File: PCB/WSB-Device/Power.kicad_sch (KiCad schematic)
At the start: 38 parts, among them J3 USB_C_Receptacle_USB2.0_14P, J4 Conn_01x02, SW2 SW_SPST_4_PIN, U2 XC6194A303ER-G, U3 USBLC6-2P6, U4 MCP73830, U6 NCP187

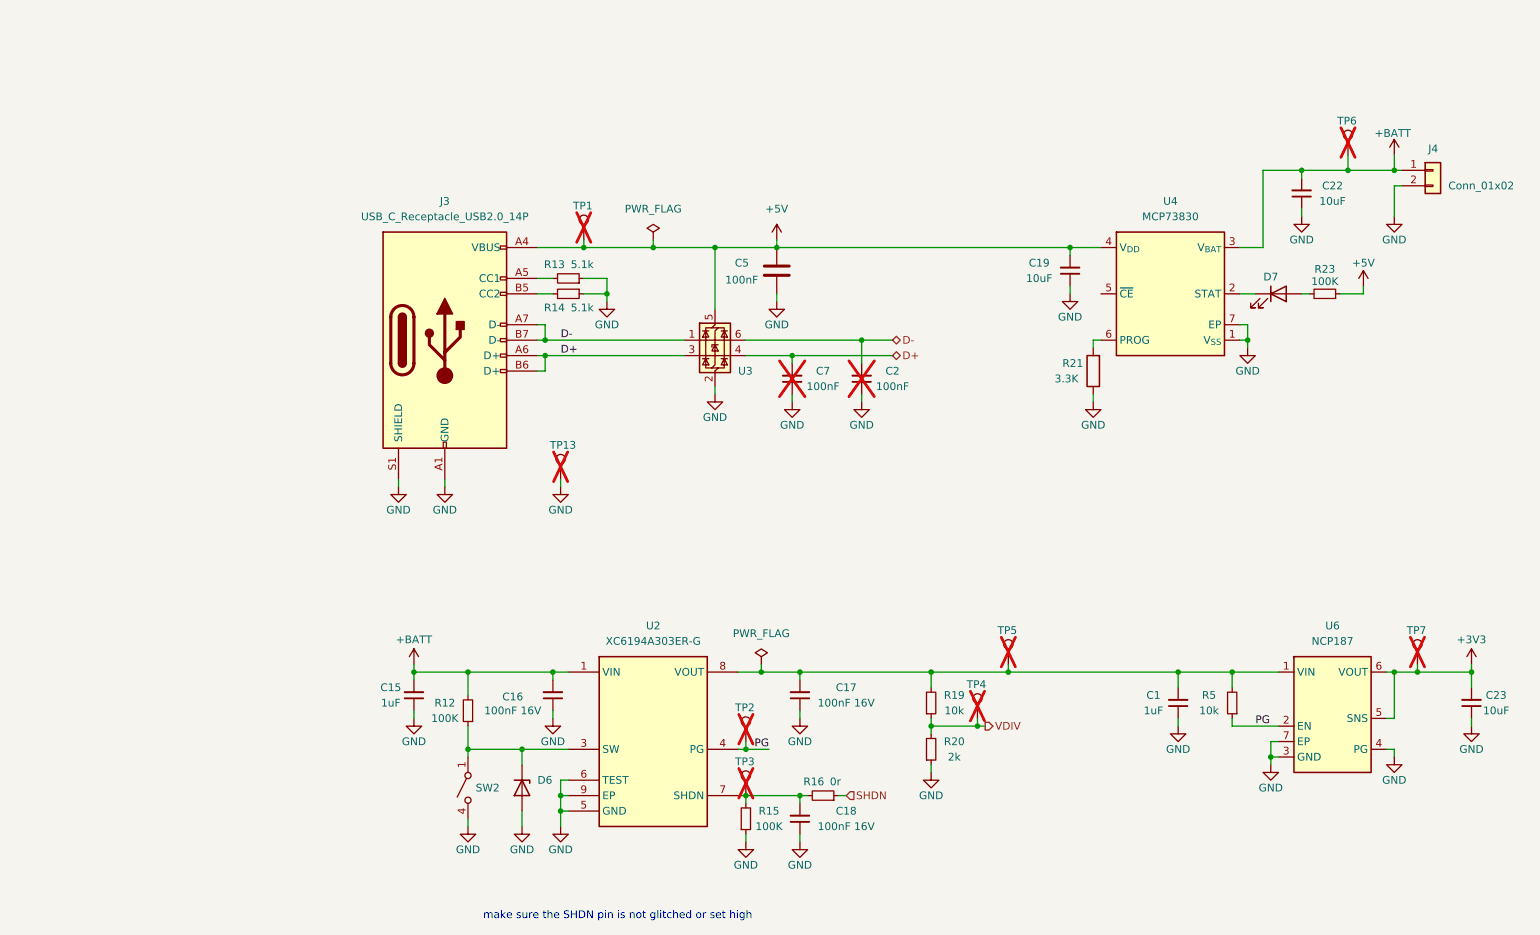
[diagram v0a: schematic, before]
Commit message: -Corrected test point numbering
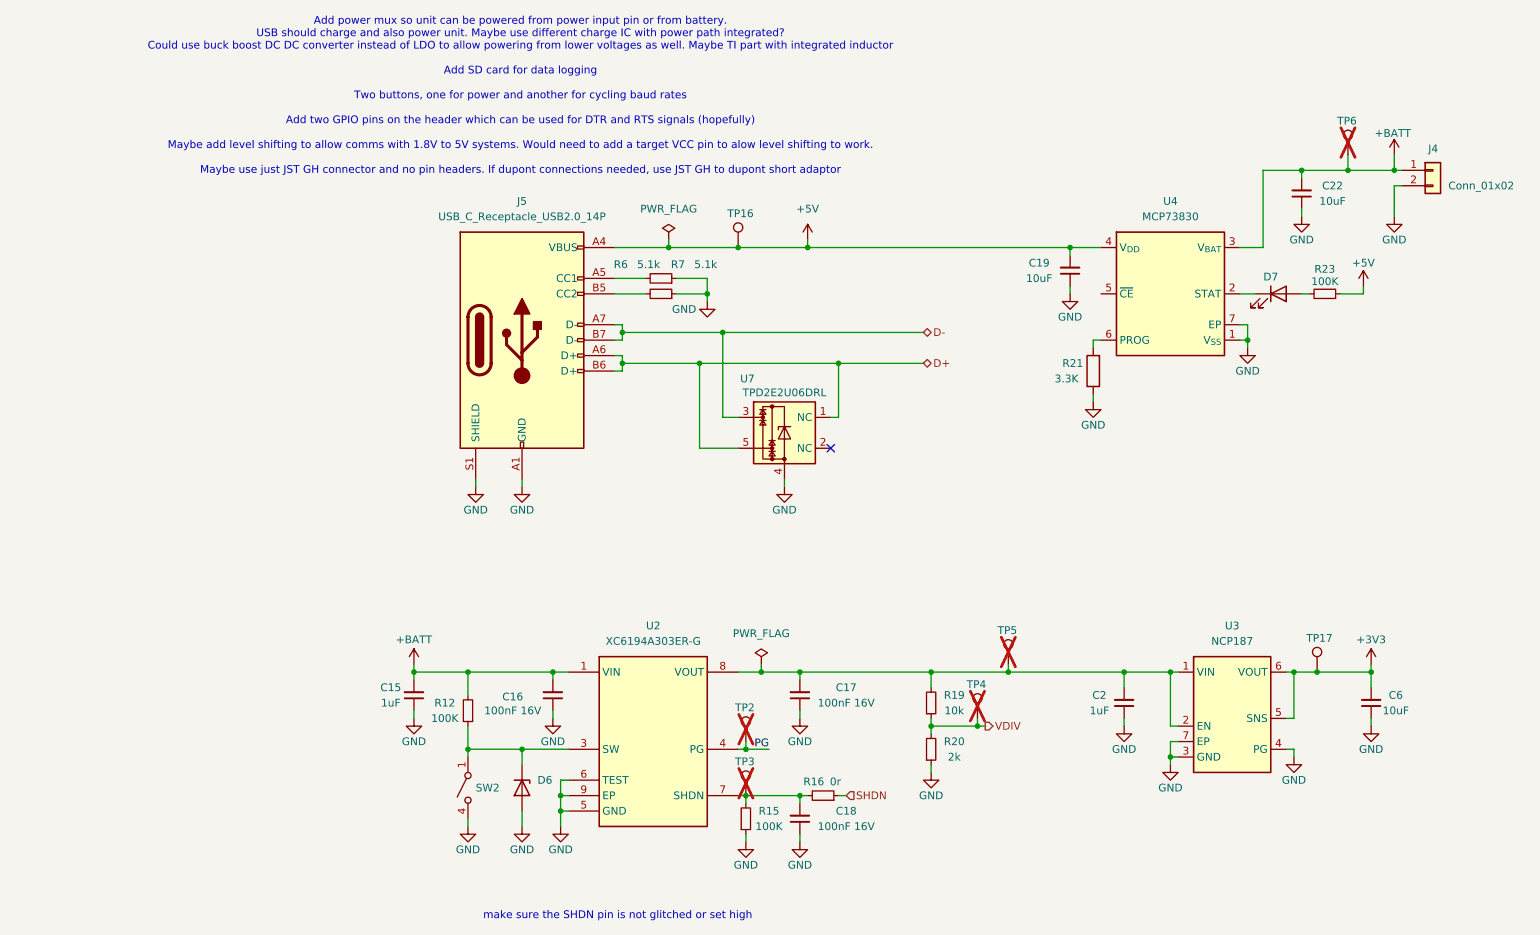
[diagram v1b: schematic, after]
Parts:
- removed C1: 1uF, Capacitor_SMD:C_0402_1005Metric, symbol Device:C_Small
- removed C23: 10uF, Capacitor_SMD:C_0603_1608Metric, symbol Device:C_Small
- removed C5: 100nF, Capacitor_SMD:C_0402_1005Metric, symbol Device:C
- removed C7: 100nF, Capacitor_SMD:C_0402_1005Metric, symbol Device:C_Small
- removed J3: USB_C_Receptacle_USB2.0_14P, Connector_USB:USB_C_Receptacle_G-Switch_GT-USB-7010ASV, symbol Connector:USB_C_Receptacle_USB2.0_14P
- removed R13, R14: 5.1k, Resistor_SMD:R_0402_1005Metric, symbol Device:R_Small
- removed R5: 10k, Resistor_SMD:R_0402_1005Metric, symbol Device:R_Small
- removed TP1, TP13, TP7: TestPoint, TestPoint:TestPoint_Pad_D1.0mm, symbol Connector:TestPoint
- removed U3: USBLC6-2P6, EN_Designs-Footprints:ST_SOT-666, symbol Power_Protection:USBLC6-2P6
- removed U6: NCP187, EN_Designs-Footprints:OnSemi_WDFN6_2x2_0.65P_CASE_511BR, symbol EN_Designs-Symbols:NCP187
- added C6: 10uF, Capacitor_SMD:C_0603_1608Metric, symbol Device:C_Small
- added J5: USB_C_Receptacle_USB2.0_14P, Connector_USB:USB_C_Receptacle_G-Switch_GT-USB-7010ASV, symbol Connector:USB_C_Receptacle_USB2.0_14P
- added R6, R7: 5.1k, Resistor_SMD:R_0201_0603Metric, symbol Device:R_Small
- added TP16, TP17: TestPoint, EN_Designs-Footprints:TestPoint_Pad_D1.0mm, symbol Connector:TestPoint
- added U3: NCP187, EN_Designs-Footprints:OnSemi_WDFN6_2x2_0.65P_CASE_511BR, symbol EN_Designs-Symbols:NCP187
- added U7: TPD2E2U06DRL, Package_TO_SOT_SMD:SOT-553, symbol Power_Protection:TPD2E2U06DRL
- C2: value 100nF -> 1uF; now fitted
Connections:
- net +3V3: now also C6.2, TP17.1, U3.5 (SNS), U3.6 (VOUT)
- net +5V: now also J5.A4 (VBUS), J5.A9 (VBUS), J5.B4 (VBUS), J5.B9 (VBUS), TP16.1
- net D+: now also J5.A6 (D+), J5.B6 (D+), U7.1 (NC), U7.5
- net D-: now also J5.A7 (D-), J5.B7 (D-), U7.3; no longer C2.2
- net GND: now also C6.1, J5.A1 (GND), J5.A12 (GND), J5.B1 (GND), J5.B12 (GND), J5.S1 (SHIELD), R6.1, R7.1, U3.3 (GND), U3.4 (PG), U3.7 (EP), U7.4
- net at C17.2, R19.2, TP5.1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: now also C2.2, U3.1 (VIN), U3.2 (EN)
- new net: J5.B5 (CC2), R7.2
- new net: J5.A5 (CC1), R6.2
- no-connect marks 0 -> 1
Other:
- note added: "Add power mux so unit can be powered from power input pin or from battery. USB should charge and also power unit. Maybe use different charge IC with power path integrated? Could use buck boost DC DC converter instead of LDO to allow powering from lower voltages as well. Maybe TI part with integrated inductor Add SD card for data logging Two buttons, one for power and another for cycling baud rate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"
